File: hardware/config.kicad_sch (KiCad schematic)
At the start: 38 parts, among them J4 JTAG, SW1 219-2MST, U4 GateMate-CCGM1A1, U9 AT25QL321-MBUE-T

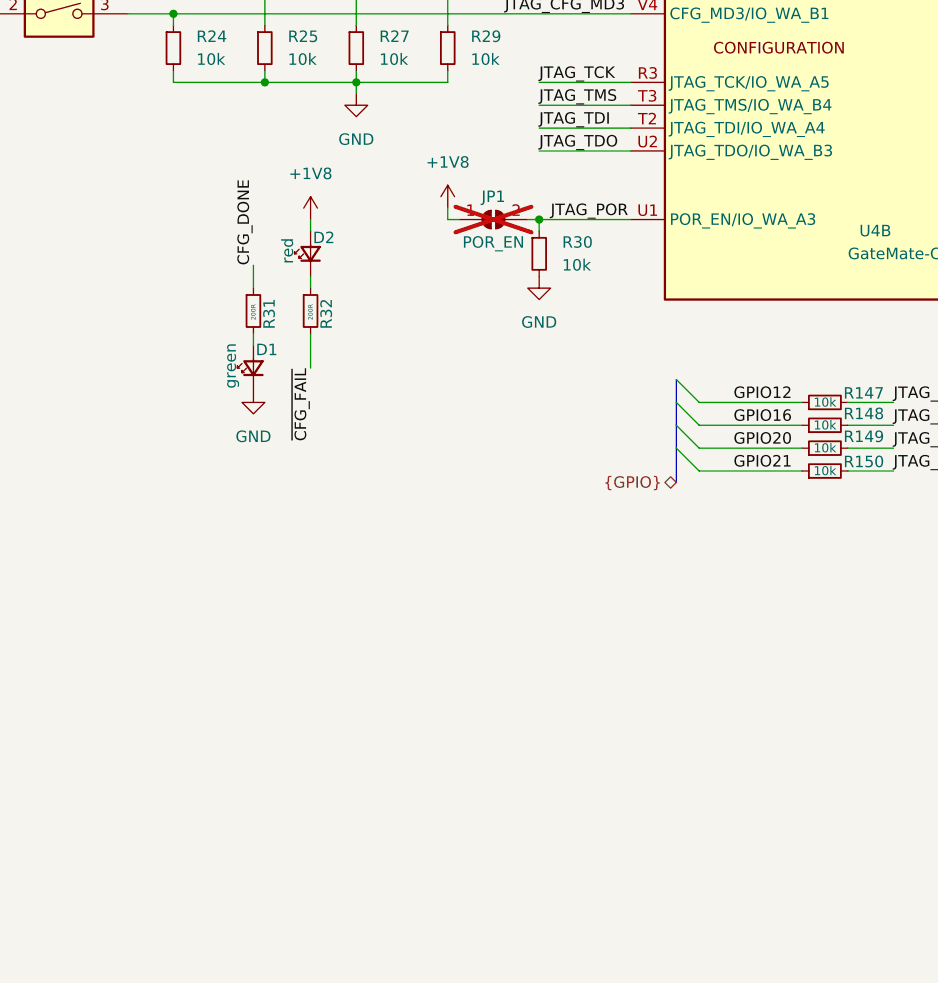
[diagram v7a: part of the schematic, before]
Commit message: #26 Added to schematics and PCB but not connected, placed, routed
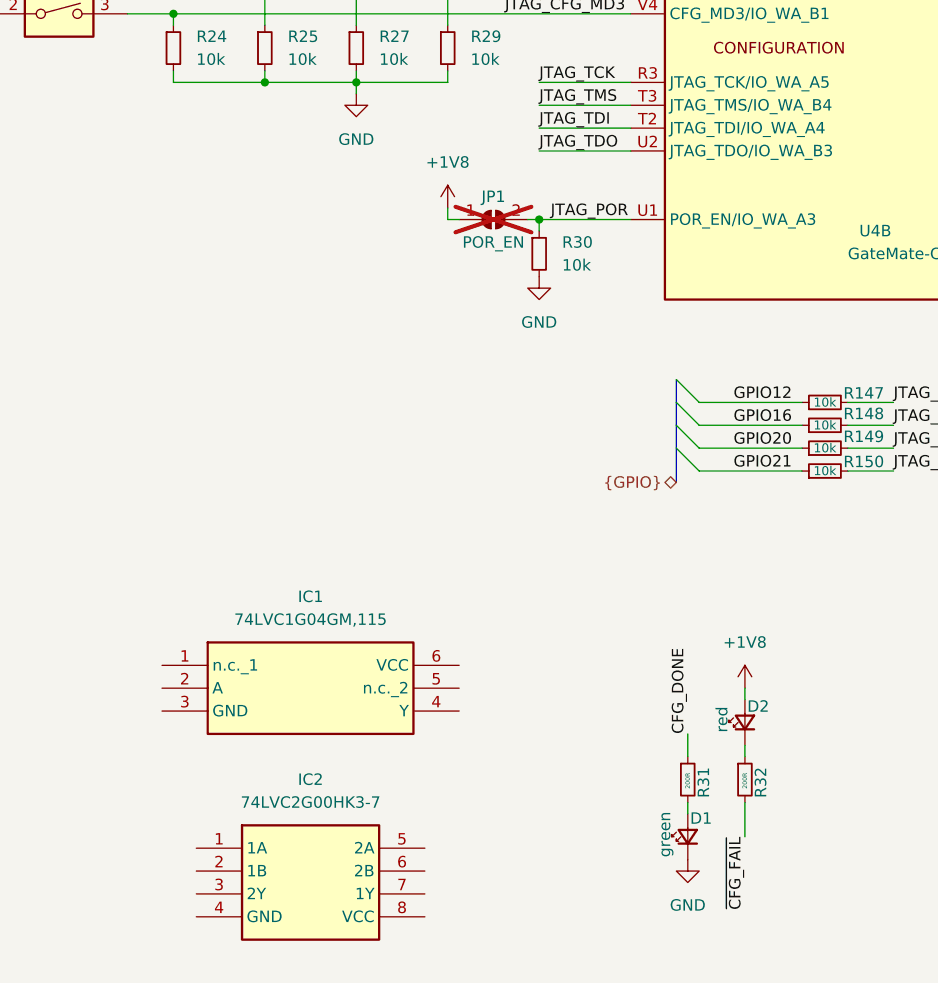
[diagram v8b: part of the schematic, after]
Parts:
- added IC1: 74LVC1G04GM,115, 74LVC1G04GM,115:PESD3V3L5UF115, symbol 74LVC1G04GM_115:74LVC1G04GM,115
- added IC2: 74LVC2G00HK3-7, 74LVC2G00HK3-7:74LVC2G00HK37, symbol 74LVC2G00HK3-7:74LVC2G00HK3-7
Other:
- moved on the sheet: D1, D2, R31, R32
